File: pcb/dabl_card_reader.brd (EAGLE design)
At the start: 160 x 100 mm, 2 parts, among them U1 TEENSY_3.1_WITH_AUDIO

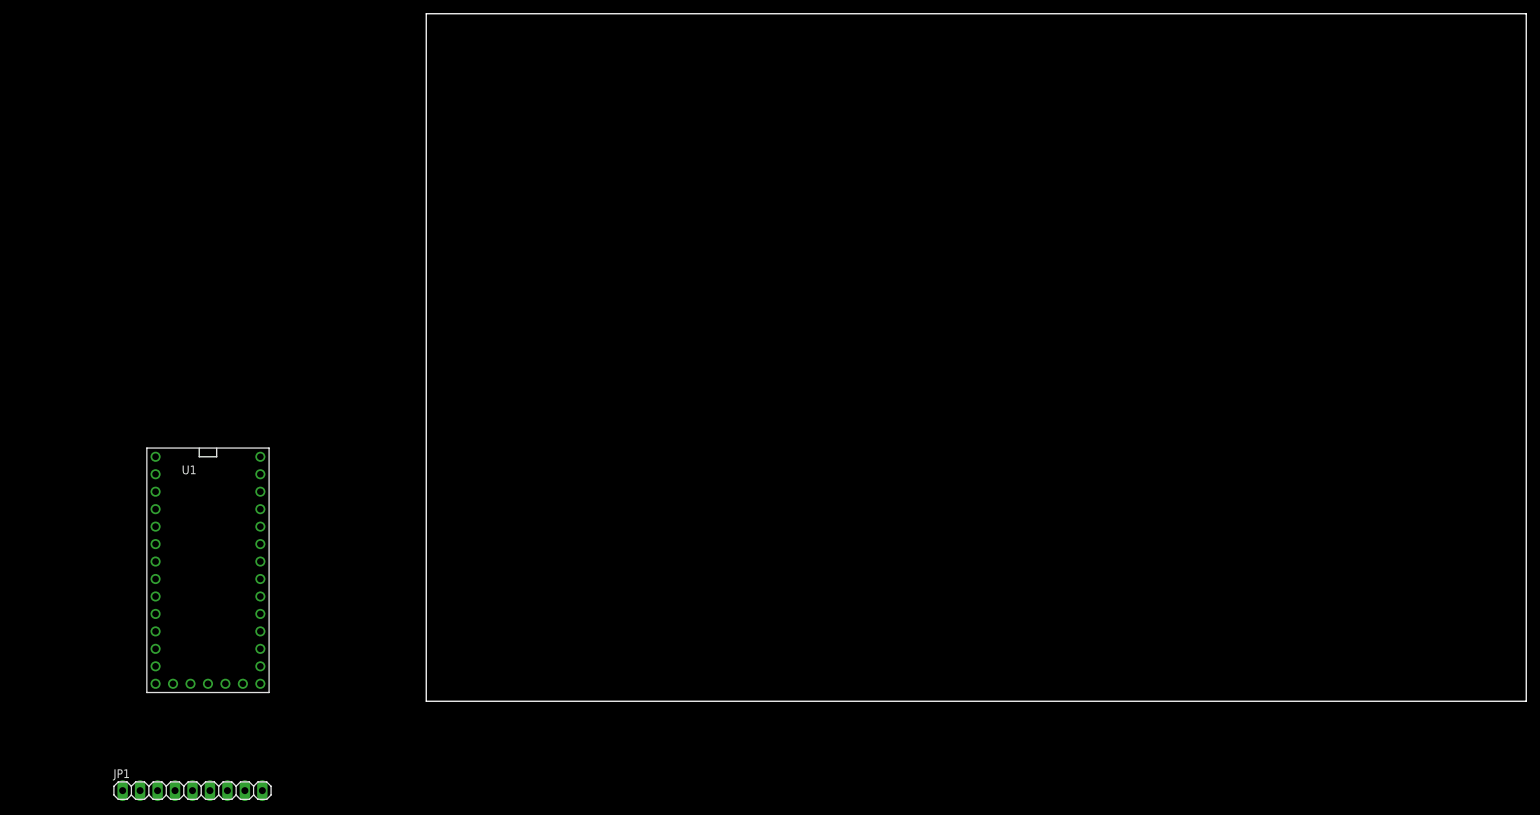
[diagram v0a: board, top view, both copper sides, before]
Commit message: pulled in PN532 board dimensions and pin layout
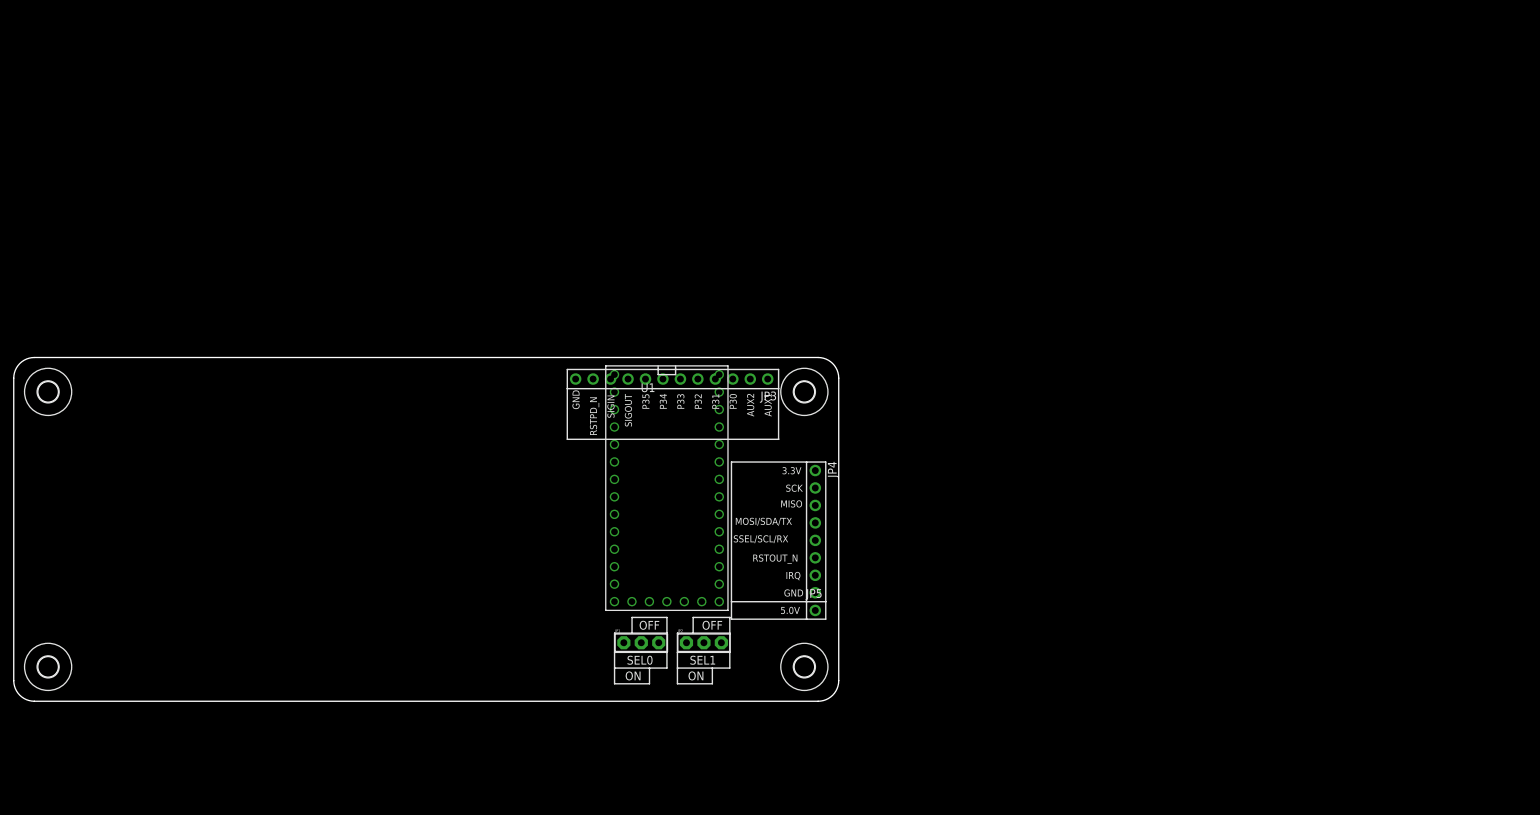
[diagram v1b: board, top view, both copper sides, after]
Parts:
- added JP2: SEL1, microbuilder:JUMPER3
- added JP3: (no value), microbuilder:1X12_ROUND
- added JP4: (no value), microbuilder:1X08_ROUND
- added JP5: (no value), microbuilder:1X01_ROUND
- added U$36, U$37, U$38, U$6: (no value), microbuilder:MOUNTINGHOLE_3.0
- JP1: value (none) -> SEL0; device pinhead:1X09 -> microbuilder:JUMPER3
- moved JP1 68.7 mm to (31.3, 8.51)
- moved U1 67.8 mm to (35.0, 31.0)
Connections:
- new net IRQ: JP4.7
- new net MISO: JP4.3
- new net MOSI/SDA/TX: JP4.4
- new net NSS/SCL/RX: JP4.5
- new net RSTOUT_N: JP4.6
- new net SCK: JP4.2
- new net SEL0: JP1.2
- new net SEL1: JP2.2
- new net VDD: JP1.1, JP2.1, JP4.1
- net GND: now also JP1.3, JP2.3, JP3.12, JP4.8
- net VIN: now also JP5.1
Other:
- board size 160 x 100 mm -> 120 x 50 mm
- board text added: "3.3V"
- board text added: "5.0V"
- board text added: "AUX1"
- board text added: "AUX2"
- board text added: "GND"
- board text added: "IRQ"
- board text added: "MISO"
- board text added: "MOSI/SDA/TX"
- board text added: "OFF"
- board text added: "ON"
- board text added: "P30"
- board text added: "P31"
- board text added: "P32"
- board text added: "P33"
- board text added: "P34"
- board text added: "P35"
- board text added: "RSTOUT_N"
- board text added: "RSTPD_N"
- board text added: "SCK"
- board text added: "SEL0"
- board text added: "SEL1"
- board text added: "SIGIN"
- board text added: "SIGOUT"
- board text added: "SSEL/SCL/RX"

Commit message: full pcb for testing
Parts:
- removed U$36, U$6: (no value), microbuilder:MOUNTINGHOLE_3.0
- added JP6: (no value), pinhead:1X02
- added R1, R2, R3: 220, resistor:0207/10
- JP3: device microbuilder:1X12_ROUND -> pinhead:1X04
- moved JP3 39.3 mm to (22.0, 10.0), turned to 270 degrees
- moved U1 4.12 mm to (39.0, 32.0)
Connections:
- removed net 3.3V: U1.3.3V, U1.3.3V1
- removed net MOSI/SDA/TX: JP4.4
- removed net NSS/SCL/RX: JP4.5
- removed net SEL0: JP1.2
- removed net SEL1: JP2.2
- new net CS: JP4.5, U1.10
- new net MOSI: JP4.4, U1.11
- new net N$1: JP3.4, R3.1
- new net N$10: R1.2, U1.14/A0
- new net N$2: JP3.3, R2.1
- new net N$5: JP3.1, R1.1
- new net N$8: R3.2, U1.16/A2
- new net N$9: R2.2, U1.15/A1
- net GND: now also JP1.2, JP3.2, JP6.2; no longer JP3.12
- net MISO: now also U1.12
- net SCK: now also U1.13
- net VDD: now also JP2.2, U1.3.3V, U1.3.3V1
- net VIN: no longer JP5.1
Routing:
- net VDD: track 0.00 -> 71.5 mm, vias 0 -> 1
- net MISO: track 0.00 -> 30.6 mm, vias 0 -> 1
- net CS: track 0.00 -> 29.6 mm, vias 0 -> 1
- net N$10: track 0.00 -> 29.4 mm
- net MOSI: track 0.00 -> 28.5 mm, vias 0 -> 1
- net N$9: track 0.00 -> 25.1 mm
- net SCK: track 0.00 -> 21.2 mm, vias 0 -> 1
- net N$8: track 0.00 -> 21.1 mm
- net N$1: track 0.00 -> 15.2 mm
- net N$2: track 0.00 -> 11.4 mm
- net N$5: track 0.00 -> 5.11 mm
- added copper zone on layer 1, net GND
- added copper zone on layer 16, net GND
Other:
- board size 120 x 50 mm -> 42 x 50 mm

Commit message: finish initial pcb design
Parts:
- added ESP8266: (no value), pinhead:2X04
- R1, R2, R3: device resistor:0207/10 -> resistor:M0805
- moved R3 8.49 mm to (22.0, 18.0)
- moved R1 7.21 mm to (26.0, 18.0)
- moved R2 6.08 mm to (24.0, 18.0)
- flipped LED to the bottom, turned to 90 degrees
- flipped TEENSY to the bottom
- renumbered JP3 to LED, JP4 to SHIELD_PN532, JP6 to SHIELD_GND, U1 to TEENSY
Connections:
- removed net N$10: R1.2, TEENSY.14/A0
- removed net N$8: R3.2, TEENSY.16/A2
- removed net N$9: R2.2, TEENSY.15/A1
- removed net VDD: JP1.1, JP2.1, JP2.2, SHIELD_PN532.1, TEENSY.3.3V, TEENSY.3.3V1
- new net 3.3V: ESP8266.2, JP1.1, JP2.1, JP2.2, SHIELD_PN532.1, TEENSY.3.3V, TEENSY.3.3V1
- new net ESP_CHEN: ESP8266.6, TEENSY.6
- new net ESP_GPIO0: ESP8266.3, TEENSY.7
- new net ESP_GPIO2: ESP8266.5, TEENSY.8
- new net ESP_RST: ESP8266.4, TEENSY.2
- new net ESP_RX: ESP8266.1, TEENSY.1
- new net ESP_TX: ESP8266.8, TEENSY.0
- new net LED_B: R3.2, TEENSY.5
- new net LED_G: R2.2, TEENSY.4
- new net LED_R: R1.2, TEENSY.3
- net GND: now also ESP8266.7
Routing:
- net 3.3V: track 0.00 -> 116.3 mm, vias 0 -> 2
- net VDD: track 71.5 -> 0.00 mm, vias 1 -> 0
- net LED_R: track 0.00 -> 43.6 mm
- net LED_G: track 0.00 -> 40.8 mm
- net LED_B: track 0.00 -> 37.9 mm
- net ESP_RX: track 0.00 -> 36.4 mm, vias 0 -> 2
- net ESP_GPIO2: track 0.00 -> 35.7 mm
- net N$10: track 29.4 -> 0.00 mm
- net ESP_RST: track 0.00 -> 29.0 mm
- net ESP_TX: track 0.00 -> 25.6 mm
- net N$9: track 25.1 -> 0.00 mm
- net ESP_GPIO0: track 0.00 -> 24.9 mm
- net ESP_CHEN: track 0.00 -> 22.4 mm
- net N$8: track 21.1 -> 0.00 mm
- net CS: track 29.6 -> 11.2 mm
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
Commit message: fix pcb traces
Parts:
- flipped ESP8266 to the top, turned to 270 degrees
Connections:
- net 3.3V: now also ESP8266.8; no longer ESP8266.2
- net ESP_CHEN: now also ESP8266.4; no longer ESP8266.6
- net ESP_GPIO0: now also ESP8266.5; no longer ESP8266.3
- net ESP_GPIO2: now also ESP8266.3; no longer ESP8266.5
- net ESP_RST: now also ESP8266.6; no longer ESP8266.4
- net ESP_RX: now also ESP8266.7; no longer ESP8266.1
- net ESP_TX: now also ESP8266.2; no longer ESP8266.8
- net GND: now also ESP8266.1; no longer ESP8266.7
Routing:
- net LED_R: track 43.6 -> 44.5 mm
